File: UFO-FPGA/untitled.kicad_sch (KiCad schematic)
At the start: 16 parts, among them U4 MC34063AD

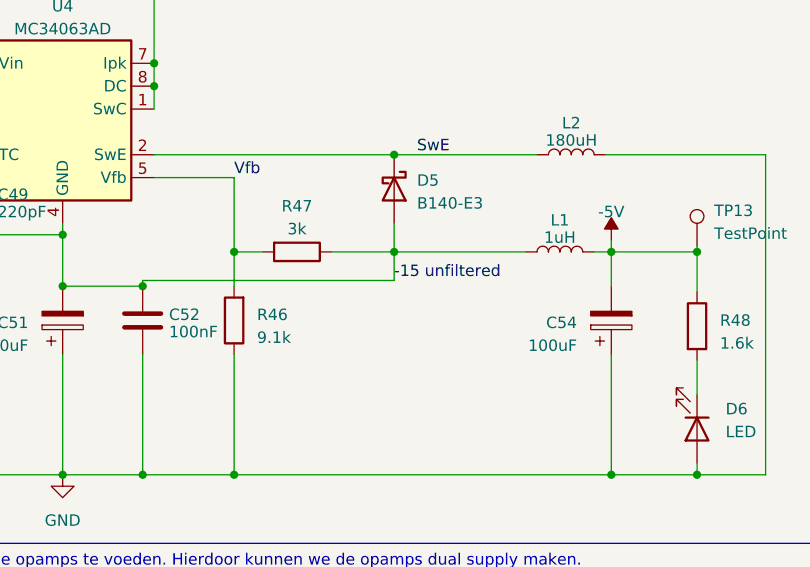
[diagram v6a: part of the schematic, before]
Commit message: Weerstanden waardes verandert en namen verandert
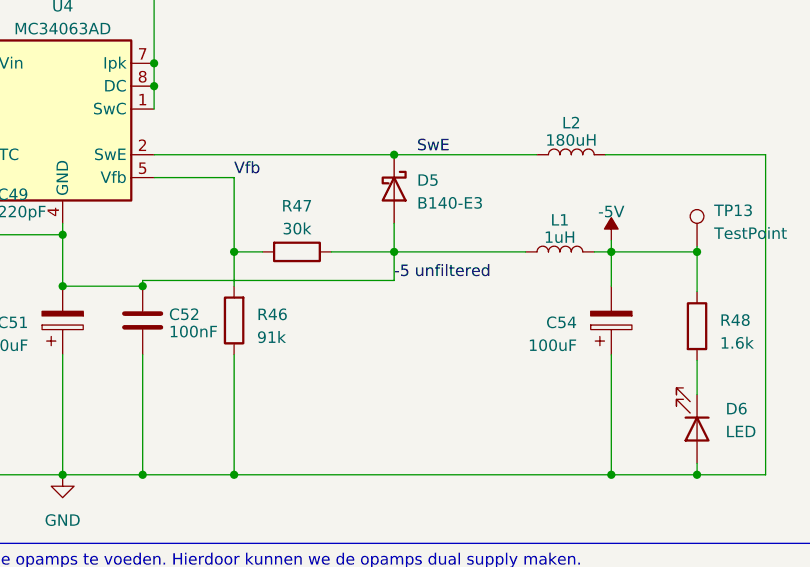
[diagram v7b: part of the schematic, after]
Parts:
- R46: value 9.1k -> 91k
- R47: value 3k -> 30k
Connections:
- net -15 unfiltered renamed -5 unfiltered
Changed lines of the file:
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@@
     (effects (font (size 1.27 1.27)) (justify left top))
   )
-  (label "-15 unfiltered" (at 168.91 104.14 0) (fields_autoplaced)
+  (label "-5 unfiltered" (at 168.91 104.14 0) (fields_autoplaced)
     (effects (font (size 1.27 1.27)) (justify left bottom))
   )
@@
       (effects (font (size 1.27 1.27)) (justify right))
     )
-    (property "Value" "9.1k" (at 153.67 110.49 0)
+    (property "Value" "91k" (at 153.67 110.49 0)
       (effects (font (size 1.27 1.27)) (justify right))
     )
@@
       (effects (font (size 1.27 1.27)))
     )
-    (property "Value" "3k" (at 158.115 98.425 90)
+    (property "Value" "30k" (at 158.115 98.425 90)
       (effects (font (size 1.27 1.27)))
     )

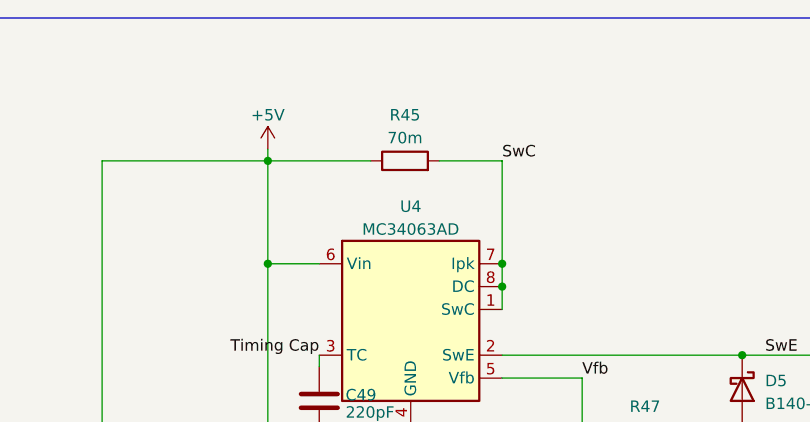
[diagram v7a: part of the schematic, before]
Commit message: Weerstand veranderd Waardoor er minder stroom loopt naar de opamp want er is niet veel stroom nodig
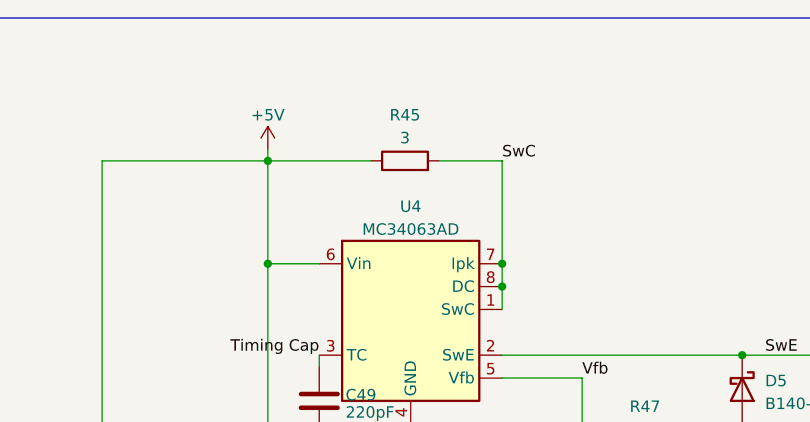
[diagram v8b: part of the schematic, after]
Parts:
- R45: value 70m -> 3
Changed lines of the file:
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@@
       (effects (font (size 1.27 1.27)))
     )
-    (property "Value" "70m" (at 131.445 66.04 90)
+    (property "Value" "3" (at 131.445 66.04 90)
       (effects (font (size 1.27 1.27)))
     )
